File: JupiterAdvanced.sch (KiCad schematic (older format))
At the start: 224 parts, among them SW1 SW_Push, U1 PRTR5V0U2X, U10 ATmega32U4-AU, Y1 16MHz

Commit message: Rerouting for atmega32u4 complete
and its a complete mess...
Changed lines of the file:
@@
 Text GLabel 12300 3550 2    50   Input ~ 0
 COL15
+Text GLabel 12300 2550 2    50   Input ~ 0
+ROW6
 Text GLabel 12300 2650 2    50   Input ~ 0
-ROW6
-Text GLabel 12300 2450 2    50   Input ~ 0
 ROW0
 Text GLabel 12300 3250 2    50   Input ~ 0
@@
 Wire Wire Line
 	9850 2450 9750 2450
-Text GLabel 12300 2550 2    50   Input ~ 0
+Text GLabel 12300 2450 2    50   Input ~ 0
 ROW5
 $EndSCHEMATC

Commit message: Push switch updated for JLCPCB
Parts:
- SW1: footprint random-keyboard-parts:SKQG-1155865 -> JupiterAdvancedKbd_localFP:TS-1187A-B-A-B; LCSC (none) -> C318884
- U10: LCSC (none) -> C44854
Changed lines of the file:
@@
 F 0 "SW1" H 10650 2385 50  0000 C CNN
 F 1 "SW_Push" H 10650 2294 50  0000 C CNN
-F 2 "random-keyboard-parts:SKQG-1155865" H 10650 2300 50  0001 C CNN
+F 2 "JupiterAdvancedKbd_localFP:TS-1187A-B-A-B" H 10650 2300 50  0001 C CNN
 F 3 "~" H 10650 2300 50  0001 C CNN
+F 4 "C318884" H 10650 2100 50  0001 C CNN "LCSC"
 	1    10650 2100
 	1    0    0    -1
@@
 F 2 "Package_QFP:TQFP-44_10x10mm_P0.8mm" H 11700 3850 50  0001 C CIN
 F 3 "http://ww1.microchip.com/downloads/en/DeviceDoc/Atmel-7766-8-bit-AVR-ATmega16U4-32U4_Datasheet.pdf" H 11700 3850 50  0001 C CNN
+F 4 "C44854" H 11700 3850 50  0001 C CNN "LCSC"
 	1    11700 3850
 	1    0    0    -1

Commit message: JLCPCB Order SMT0210420181311
SMT0210420181311-3234210A
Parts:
- FB1: footprint Inductor_SMD:L_0805_2012Metric -> Inductor_SMD:L_1206_3216Metric; LCSC (none) -> C131463
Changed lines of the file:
@@
 F 0 "FB1" V 5613 2850 50  0000 C CNN
 F 1 "60@100MHz" V 5704 2850 50  0000 C CNN
-F 2 "Inductor_SMD:L_0805_2012Metric" V 5780 2850 50  0001 C CNN
+F 2 "Inductor_SMD:L_1206_3216Metric" V 5780 2850 50  0001 C CNN
 F 3 "~" H 5850 2850 50  0001 C CNN
+F 4 "C131463" V 5850 2850 50  0001 C CNN "LCSC"
 	1    5850 2850
 	0    1    1    0

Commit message: Cutouts in PCB created, USB port moved to protrude
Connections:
- wire segments 409 -> 407
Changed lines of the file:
@@
 D+
 Wire Wire Line
-	1450 2200 1500 2200
-Wire Wire Line
-	1550 2200 1550 2100
-Wire Wire Line
 	1550 2100 1450 2100
 Wire Wire Line
@@
 Wire Wire Line
 	2000 1100 2150 1100
-$Comp
-L power:PWR_FLAG #FLG0103
-U 1 1 6097A832
-P 1500 2200
-F 0 "#FLG0103" H 1500 2275 50  0001 C CNN
-F 1 "PWR_FLAG" H 1500 2373 50  0000 C CNN
-F 2 "" H 1500 2200 50  0001 C CNN
-F 3 "~" H 1500 2200 50  0001 C CNN
-	1    1500 2200
-	-1   0    0    1
-$EndComp
-Connection ~ 1500 2200
-Wire Wire Line
-	1500 2200 1550 2200
 Text GLabel 10800 3450 3    50   Input ~ 0
 DN
@@
 Text GLabel 12300 2450 2    50   Input ~ 0
 ROW5
+Wire Wire Line
+	1450 2200 1550 2200
+$Comp
+L power:Earth #PWR?
+U 1 1 609BA776
+P 1550 2200
+F 0 "#PWR?" H 1550 1950 50  0001 C CNN
+F 1 "Earth" H 1550 2050 50  0001 C CNN
+F 2 "" H 1550 2200 50  0001 C CNN
+F 3 "~" H 1550 2200 50  0001 C CNN
+	1    1550 2200
+	1    0    0    -1
+$EndComp
 $EndSCHEMATC

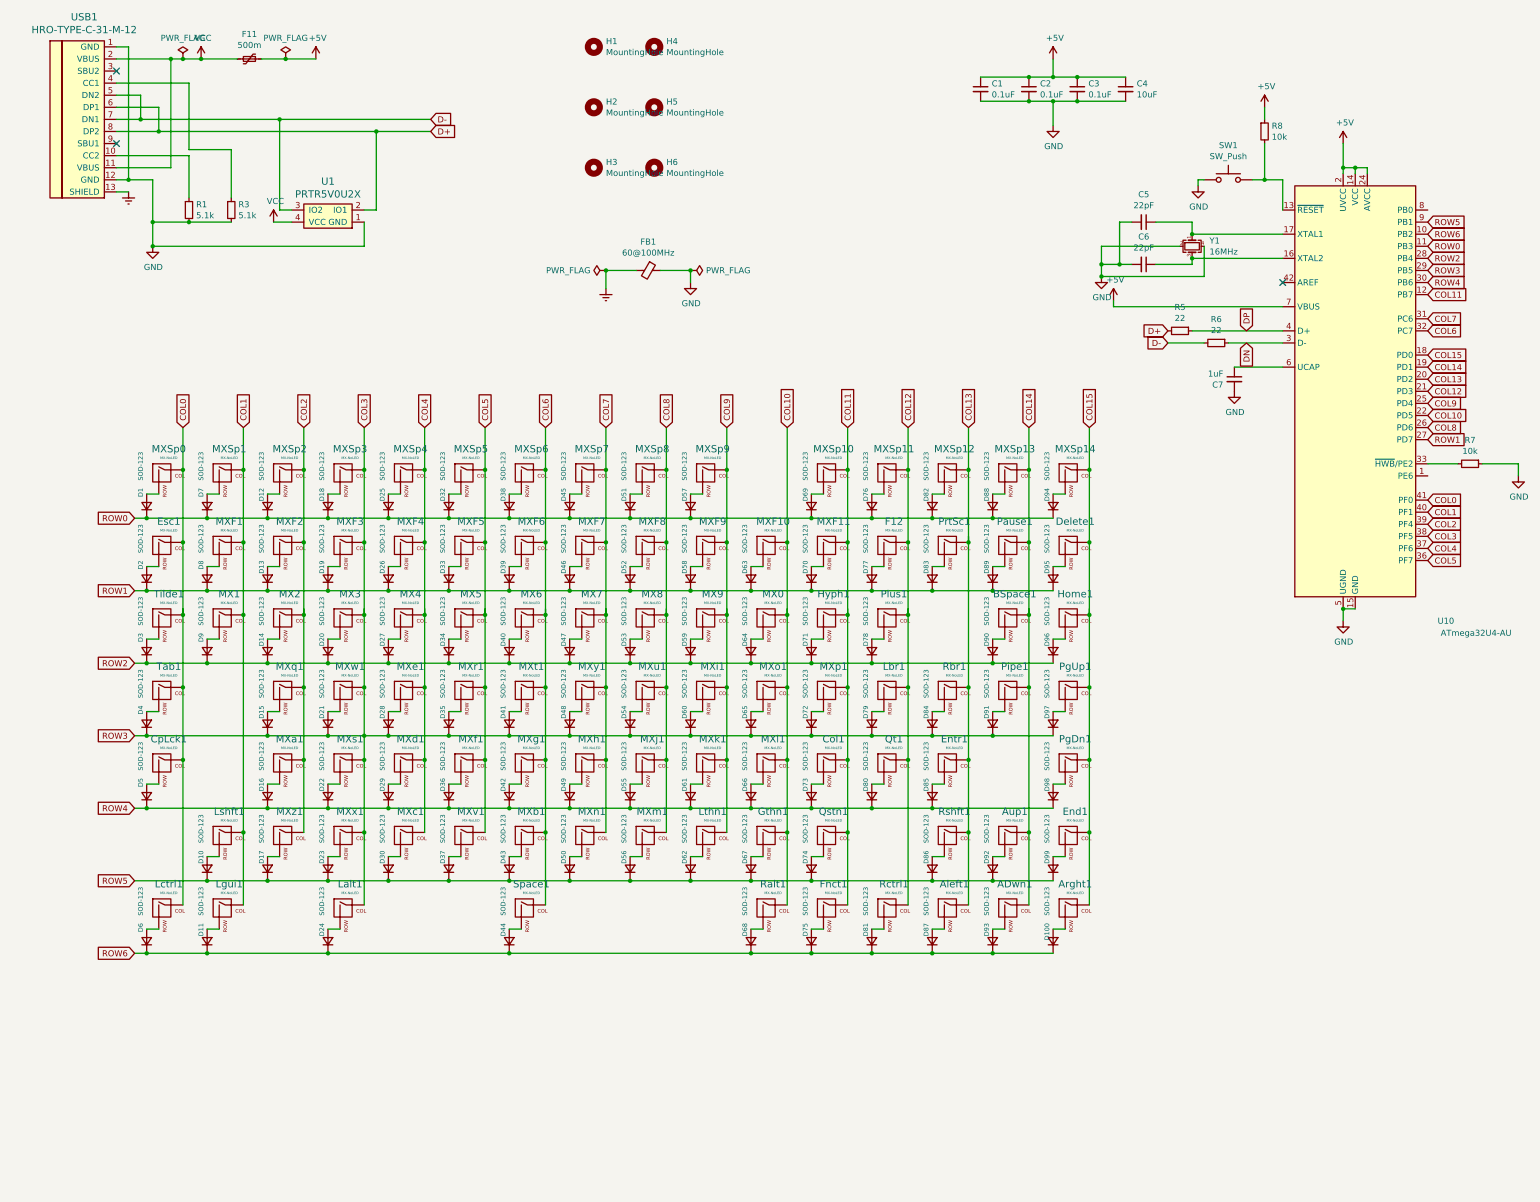
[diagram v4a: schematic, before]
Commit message: UnderGlow added, not yet routed
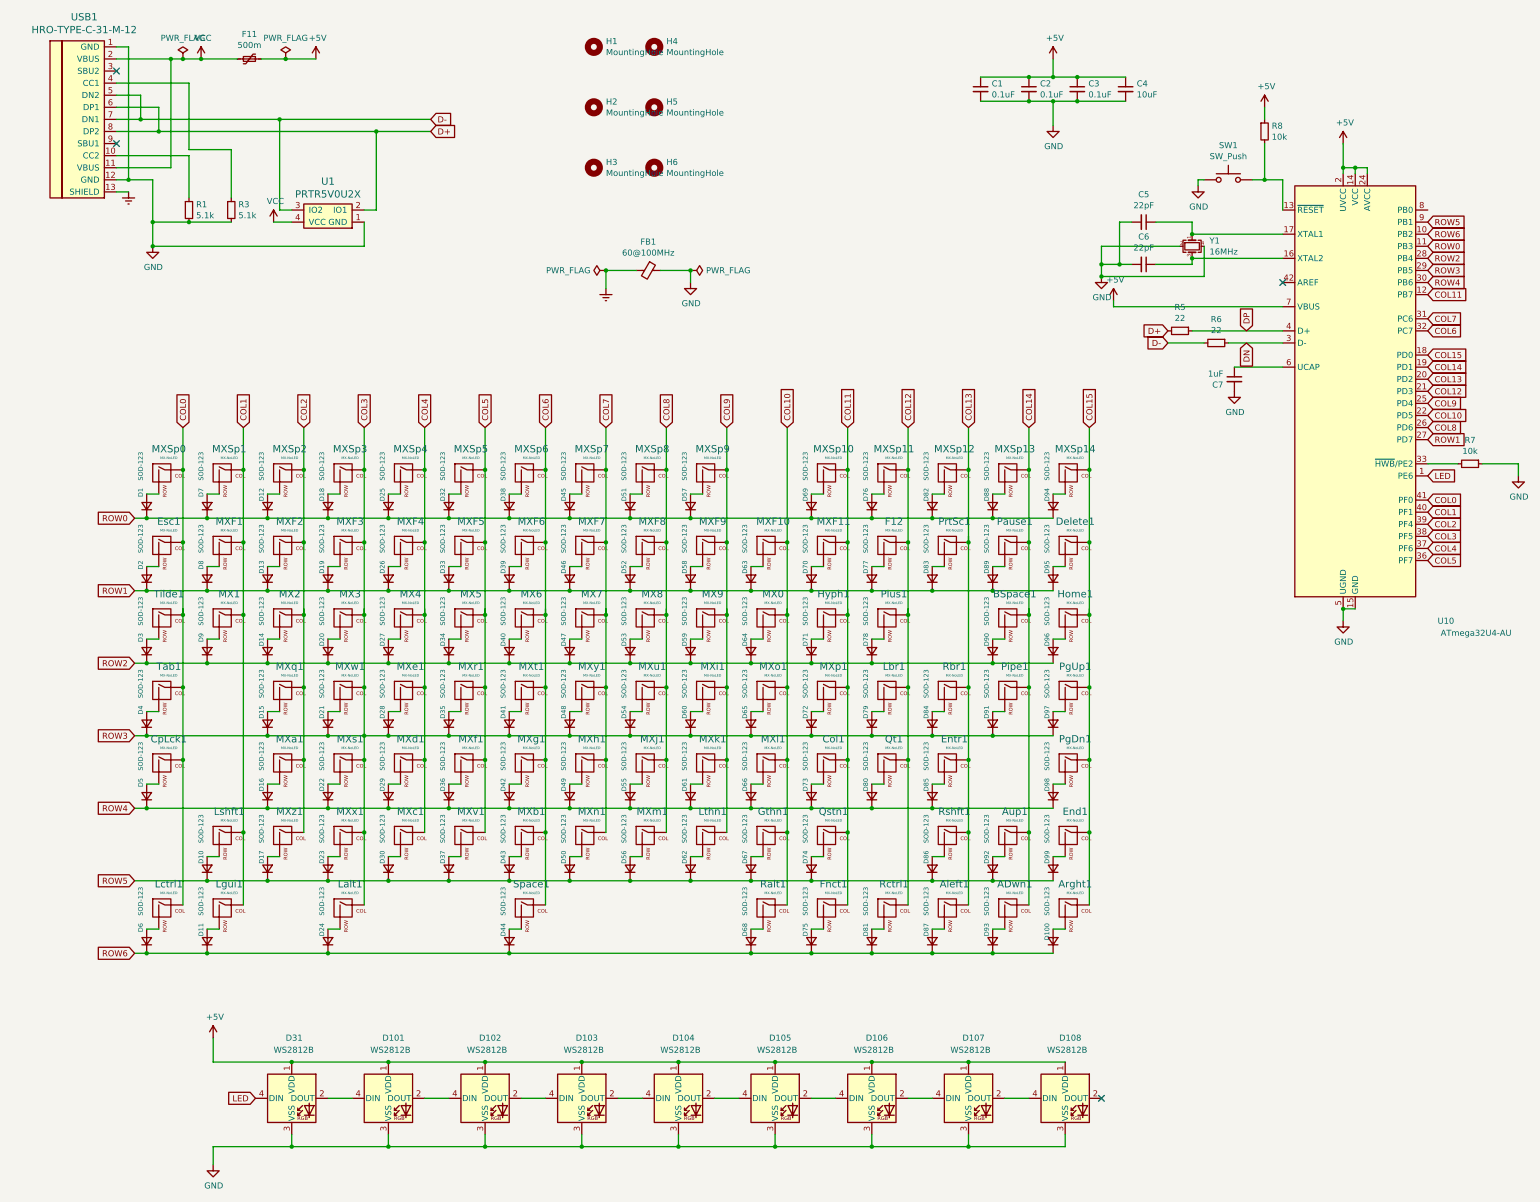
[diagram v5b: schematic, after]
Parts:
- added D101, D102, D103, D104, D105, D106, D107, D108, D31: WS2812B, LED_SMD:LED_WS2812B_PLCC4_5.0x5.0mm_P3.2mm, symbol LED:WS2812B
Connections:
- net labels added: LED
- wire segments 407 -> 444
- no-connect marks 3 -> 4
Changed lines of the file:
@@
 	1450 2200 1550 2200
 $Comp
-L power:Earth #PWR?
+L power:Earth #PWR0117
 U 1 1 609BA776
 P 1550 2200
-F 0 "#PWR?" H 1550 1950 50  0001 C CNN
+F 0 "#PWR0117" H 1550 1950 50  0001 C CNN
 F 1 "Earth" H 1550 2050 50  0001 C CNN
 F 2 "" H 1550 2200 50  0001 C CNN
@@
 	1    0    0    -1
 $EndComp
+$Comp
+L LED:WS2812B D31
+U 1 1 60A403B7
+P 2900 9700
+F 0 "D31" H 2850 10200 50  0000 L CNN
+F 1 "WS2812B" H 2750 10100 50  0000 L CNN
+F 2 "LED_SMD:LED_WS2812B_PLCC4_5.0x5.0mm_P3.2mm" H 2950 9400 50  0001 L TNN
+F 3 "https://cdn-shop.adafruit.com/datasheets/WS2812B.pdf" H 3000 9325 50  0001 L TNN
+F 4 "C114586" H 2900 9700 50  0001 C CNN "LCSC"
+	1    2900 9700
+	1    0    0    -1
+$EndComp
+$Comp
+L LED:WS2812B D101
+U 1 1 60A739C5
+P 3700 9700
+F 0 "D101" H 3650 10200 50  0000 L CNN
+F 1 "WS2812B" H 3550 10100 50  0000 L CNN
+F 2 "LED_SMD:LED_WS2812B_PLCC4_5.0x5.0mm_P3.2mm" H 3750 9400 50  0001 L TNN
+F 3 "https://cdn-shop.adafruit.com/datasheets/WS2812B.pdf" H 3800 9325 50  0001 L TNN
+F 4 "C114586" H 3700 9700 50  0001 C CNN "LCSC"
+	1    3700 9700
+	1    0    0    -1
+$EndComp
+$Comp
+L LED:WS2812B D102
+U 1 1 60A74444
+P 4500 9700
+F 0 "D102" H 4450 10200 50  0000 L CNN
+F 1 "WS2812B" H 4350 10100 50  0000 L CNN
+F 2 "LED_SMD:LED_WS2812B_PLCC4_5.0x5.0mm_P3.2mm" H 4550 9400 50  0001 L TNN
+F 3 "https://cdn-shop.adafruit.com/datasheets/WS2812B.pdf" H 4600 9325 50  0001 L TNN
+F 4 "C114586" H 4500 9700 50  0001 C CNN "LCSC"
+	1    4500 9700
+	1    0    0    -1
+$EndComp
+$Comp
+L LED:WS2812B D103
+U 1 1 60A78CF3
+P 5300 9700
+F 0 "D103" H 5250 10200 50  0000 L CNN
+F 1 "WS2812B" H 5150 10100 50  0000 L CNN
+F 2 "LED_SMD:LED_WS2812B_PLCC4_5.0x5.0mm_P3.2mm" H 5350 9400 50  0001 L TNN
+F 3 "https://cdn-shop.adafruit.com/datasheets/WS2812B.pdf" H 5400 9325 50  0001 L TNN
+F 4 "C114586" H 5300 9700 50  0001 C CNN "LCSC"
+	1    5300 9700
+	1    0    0    -1
+$EndComp
+$Comp
+L LED:WS2812B D104
+U 1 1 60A78CFE
+P 6100 9700
+F 0 "D104" H 6050 10200 50  0000 L CNN
+F 1 "WS2812B" H 5950 10100 50  0000 L CNN
+F 2 "LED_SMD:LED_WS2812B_PLCC4_5.0x5.0mm_P3.2mm" H 6150 9400 50  0001 L TNN
+F 3 "https://cdn-shop.adafruit.com/datasheets/WS2812B.pdf" H 6200 9325 50  0001 L TNN
+F 4 "C114586" H 6100 9700 50  0001 C CNN "LCSC"
+	1    6100 9700
+	1    0    0    -1
+$EndComp
+$Comp
+L LED:WS2812B D105
+U 1 1 60A78D09
+P 6900 9700
+F 0 "D105" H 6850 10200 50  0000 L CNN
+F 1 "WS2812B" H 6750 10100 50  0000 L CNN
+F 2 "LED_SMD:LED_WS2812B_PLCC4_5.0x5.0mm_P3.2mm" H 6950 9400 50  0001 L TNN
+F 3 "https://cdn-shop.adafruit.com/datasheets/WS2812B.pdf" H 7000 9325 50  0001 L TNN
+F 4 "C114586" H 6900 9700 50  0001 C CNN "LCSC"
+	1    6900 9700
+	1    0    0    -1
+$EndComp
+$Comp
+L LED:WS2812B D106
+U 1 1 60AAB8BE
+P 7700 9700
+F 0 "D106" H 7650 10200 50  0000 L CNN
+F 1 "WS2812B" H 7550 10100 50  0000 L CNN
+F 2 "LED_SMD:LED_WS2812B_PLCC4_5.0x5.0mm_P3.2mm" H 7750 9400 50  0001 L TNN
+F 3 "https://cdn-shop.adafruit.com/datasheets/WS2812B.pdf" H 7800 9325 50  0001 L TNN
+F 4 "C114586" H 7700 9700 50  0001 C CNN "LCSC"
+	1    7700 9700
+	1    0    0    -1
+$EndComp
+$Comp
+L LED:WS2812B D107
+U 1 1 60AAB8C9
+P 8500 9700
+F 0 "D107" H 8450 10200 50  0000 L CNN
+F 1 "WS2812B" H 8350 10100 50  0000 L CNN
+F 2 "LED_SMD:LED_WS2812B_PLCC4_5.0x5.0mm_P3.2mm" H 8550 9400 50  0001 L TNN
+F 3 "https://cdn-shop.adafruit.com/datasheets/WS2812B.pdf" H 8600 9325 50  0001 L TNN
+F 4 "C114586" H 8500 9700 50  0001 C CNN "LCSC"
+	1    8500 9700
+	1    0    0    -1
+$EndComp
+$Comp
+L LED:WS2812B D108
+U 1 1 60AAB8D4
+P 9300 9700
+F 0 "D108" H 9250 10200 50  0000 L CNN
+F 1 "WS2812B" H 9150 10100 50  0000 L CNN
+F 2 "LED_SMD:LED_WS2812B_PLCC4_5.0x5.0mm_P3.2mm" H 9350 9400 50  0001 L TNN
+F 3 "https://cdn-shop.adafruit.com/datasheets/WS2812B.pdf" H 9400 9325 50  0001 L TNN
+F 4 "C114586" H 9300 9700 50  0001 C CNN "LCSC"
+	1    9300 9700
+	1    0    0    -1
+$EndComp
+Wire Wire Line
+	9300 10000 9300 10100
+Wire Wire Line
+	9300 10100 8500 10100
+Wire Wire Line
+	2250 10100 2250 10250
+Wire Wire Line
+	2900 10000 2900 10100
+Connection ~ 2900 10100
+Wire Wire Line
+	2900 10100 2250 10100
+Wire Wire Line
+	3700 10000 3700 10100
+Connection ~ 3700 10100
+Wire Wire Line
+	3700 10100 2900 10100
+Wire Wire Line
+	4500 10000 4500 10100
+Connection ~ 4500 10100
+Wire Wire Line
+	4500 10100 3700 10100
+Wire Wire Line
+	5300 10000 5300 10100
+Connection ~ 5300 10100
+Wire Wire Line
+	5300 10100 4500 10100
+Wire Wire Line
+	6100 10000 6100 10100
+Connection ~ 6100 10100
+Wire Wire Line
+	6100 10100 5300 10100
+Wire Wire Line
+	6900 10000 6900 10100
+Connection ~ 6900 10100
+Wire Wire Line
+	6900 10100 6100 10100
+Wire Wire Line
+	7700 10000 7700 10100
+Connection ~ 7700 10100
+Wire Wire Line
+	7700 10100 6900 10100
+Wire Wire Line
+	8500 10000 8500 10100
+Connection ~ 8500 10100
+Wire Wire Line
+	8500 10100 7700 10100
+$Comp
+L power:GND #PWR0118
+U 1 1 60DC6080
+P 2250 10250
+F 0 "#PWR0118" H 2250 10000 50  0001 C CNN
+F 1 "GND" H 2255 10077 50  0000 C CNN
+F 2 "" H 2250 10250 50  0001 C CNN
+F 3 "" H 2250 10250 50  0001 C CNN
+	1    2250 10250
+	1    0    0    -1
+$EndComp
+Wire Wire Line
+	9300 9400 8500 9400
+Wire Wire Line
+	2250 9400 2250 9200
+Connection ~ 2900 9400
+Wire Wire Line
+	2900 9400 2250 9400
+Connection ~ 3700 9400
+Wire Wire Line
+	3700 9400 2900 9400
+Connection ~ 4500 9400
+Wire Wire Line
+	4500 9400 3700 9400
+Connection ~ 5300 9400
+Wire Wire Line
+	5300 9400 4500 9400
+Connection ~ 6100 9400
+Wire Wire Line
+	6100 9400 5300 9400
+Connection ~ 6900 9400
+Wire Wire Line
+	6900 9400 6100 9400
+Connection ~ 7700 9400
+Wire Wire Line
+	7700 9400 6900 9400
+Connection ~ 8500 9400
+Wire Wire Line
+	8500 9400 7700 9400
+$Comp
+L power:+5V #PWR0119
+U 1 1 60DFD422
+P 2250 9200
+F 0 "#PWR0119" H 2250 9050 50  0001 C CNN
+F 1 "+5V" H 2265 9373 50  0000 C CNN
+F 2 "" H 2250 9200 50  0001 C CNN
+F 3 "" H 2250 9200 50  0001 C CNN
+	1    2250 9200
+	1    0    0    -1
+$EndComp
+Text GLabel 2600 9700 0    50   Input ~ 0
+LED
+Wire Wire Line
+	3200 9700 3400 9700
+Wire Wire Line
+	4000 9700 4200 9700
+Wire Wire Line
+	4800 9700 5000 9700
+Wire Wire Line
+	5600 9700 5800 9700
+Wire Wire Line
+	6400 9700 6600 9700
+Wire Wire Line
+	7200 9700 7400 9700
+Wire Wire Line
+	8000 9700 8200 9700
+Wire Wire Line
+	8800 9700 9000 9700
+NoConn ~ 9600 9700
+Text GLabel 12300 4550 2    50   Input ~ 0
+LED
 $EndSCHEMATC
